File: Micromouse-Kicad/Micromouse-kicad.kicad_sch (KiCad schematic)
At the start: 73 parts, among them J1 SWD, J2 USB_B_Micro, J3 UARTBTH, J4 Batería, SW1 RST, SW2 BootSwitch, SW3 PowerSwitch, SW4 BTN, U1 STM32F405RGT6, U2 LM7805_TO220, U3 AMS1117-3.3, U4 SRV05-4, U5 MPU-6500, U6 DRV8833PWPR, Y1 8MHz

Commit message: Esquemático con componentes básicos
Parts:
- removed H1: M1+, symbol Mechanical:MountingHole_Pad
- removed H2: M1-, symbol Mechanical:MountingHole_Pad
- removed H3: M2+, symbol Mechanical:MountingHole_Pad
- removed H4: M2-, symbol Mechanical:MountingHole_Pad
- added C1, C2, C5, C6: 4.7uF, symbol Device:C_Small
- added C3, C4, C7, C8: 0.1uF, symbol Device:C_Small
- added J5: VL6180x, symbol Connector_Generic:Conn_01x07
- added J6: MotorEncodL, symbol Connector_Generic:Conn_01x06
- added J7: MotorEncodR, symbol Connector_Generic:Conn_01x06
- added Q1, Q2, Q3, Q4: BS170, digikey-footprints:TO-92-3, symbol dk_Transistors-FETs-MOSFETs-Single:BS170
- added R10, R17, R18, R9: 51, symbol Device:R_Small
- added R11, R12, R19, R20: 1.8K, symbol Device:R_Small
- added R13, R14, R5, R6: 100, symbol Device:R_Small
- added R15, R16, R7, R8: 47K, symbol Device:R_Small
- added U10, U7, U8, U9: TCRT5000, TCRT5000-Footprint:OPTO_TCRT5000, symbol TCRT5000:TCRT5000
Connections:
- net +3.3V: now also C1.1, C2.1, C3.1, C4.1, C5.1, C6.1, C7.1, C8.1, J5.1 (Pin_1), J6.4 (Pin_4), J7.4 (Pin_4), R10.2, R17.2, R18.2, R9.2, U10.COLL, U7.COLL, U8.COLL, U9.COLL
- net GND: now also C1.2, C2.2, C3.2, C4.2, C5.2, C6.2, C7.2, C8.2, J5.3 (Pin_3), J6.1 (Pin_1), J7.1 (Pin_1), Q1.3 (S), Q2.3 (S), Q3.3 (S), Q4.3 (S), R11.1, R12.1, R15.1, R16.1, R19.1, R20.1, R7.1, R8.1
- net I2C2_SCL: now also J5.6 (Pin_6)
- net I2C2_SDA: now also J5.7 (Pin_7)
- net LED1: no longer U1.8 (PC0)
- net LED2: no longer U1.9 (PC1)
- net LED3: no longer U1.10 (PC2)
- net LED4: no longer U1.11 (PC3)
- net LED5: no longer U1.24 (PC4)
- net LED6: no longer U1.25 (PC5)
- net FR_Emitter: now reaches U1.16 (PA2)
- net FR_Emitter: now also R5.1
- net FL_Emitter: now reaches U1.17 (PA3)
- net FL_Emitter: now also R13.1
- net R_Emitter: now reaches U1.20 (PA4)
- net R_Emitter: now also R6.1
- net L_Emitter: now reaches U1.21 (PA5)
- net L_Emitter: now also R14.1
- net TIM1_CH1: now reaches U1.41 (PA8)
- net TIM1_CH1: now also J7.3 (Pin_3)
- net TIM1_CH2: now reaches U1.42 (PA9)
- net TIM1_CH2: now also J7.2 (Pin_2)
- net ML1: now reaches U1.58 (PB6)
- net ML1: now also U6.16 (AIN1)
- net ML2: now reaches U1.59 (PB7)
- net ML2: now also U6.15 (AIN2)
- net MR1: now reaches U1.61 (PB8)
- net MR1: now also U6.9 (BIN1)
- net MR2: now reaches U1.62 (PB9)
- net MR2: now also U6.10 (BIN2)
- net OutMR2: now reaches U6.5 (BOUT2)
- net OutMR2: now also J7.5 (Pin_5)
- net OutML1: now reaches U6.2 (AOUT1)
- net OutML1: now also J6.6 (Pin_6)
- net OutML2: now reaches U6.4 (AOUT2)
- net OutML2: now also J6.5 (Pin_5)
- net OutMR1: now reaches U6.7 (BOUT1)
- net OutMR1: now also J7.6 (Pin_6)
- net M1+ renamed TIM8_CH1
- net TIM8_CH1: now also J6.3 (Pin_3); no longer U6.16 (AIN1)
- net M1- renamed TIM8_CH2
- net TIM8_CH2: now also J6.2 (Pin_2); no longer U6.15 (AIN2)
- net M2+: no longer names the net of U1.39 (PC8)
- net M2+: no longer U6.9 (BIN1)
- net M2-: no longer names the net of U1.40 (PC9)
- net M2-: no longer U6.10 (BIN2)
- new net: Q2.2 (G), R6.2, R8.2
- new net: R18.1, U10.A
- new net: Q3.1 (D), U9.CATH
- new net: Q3.2 (G), R13.2, R15.2
- new net: Q4.2 (G), R14.2, R16.2
- new net: Q1.2 (G), R5.2, R7.2
- new net: R9.1, U7.A
- new net: Q1.1 (D), U7.CATH
- new net: Q4.1 (D), U10.CATH
- new net: R17.1, U9.A
- new net: R10.1, U8.A
- new net: Q2.1 (D), U8.CATH
- new net FL_Reciever: R19.2, U1.9 (PC1), U9.E
- new net FR_Reciever: R11.2, U1.8 (PC0), U7.E
- new net L_Reciever: R20.2, U1.11 (PC3), U10.E
- new net R_Reciever: R12.2, U1.10 (PC2), U8.E
- no-connect marks 14 -> 17
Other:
- note added: "IR Sensors"
- note added: "STM32"
- note added: "Sensor distancia - Frontal"
- moved on the sheet: CH1, CH2, D2, J2, J4, RB2, RU1, RU2, RU3, U1, Y1

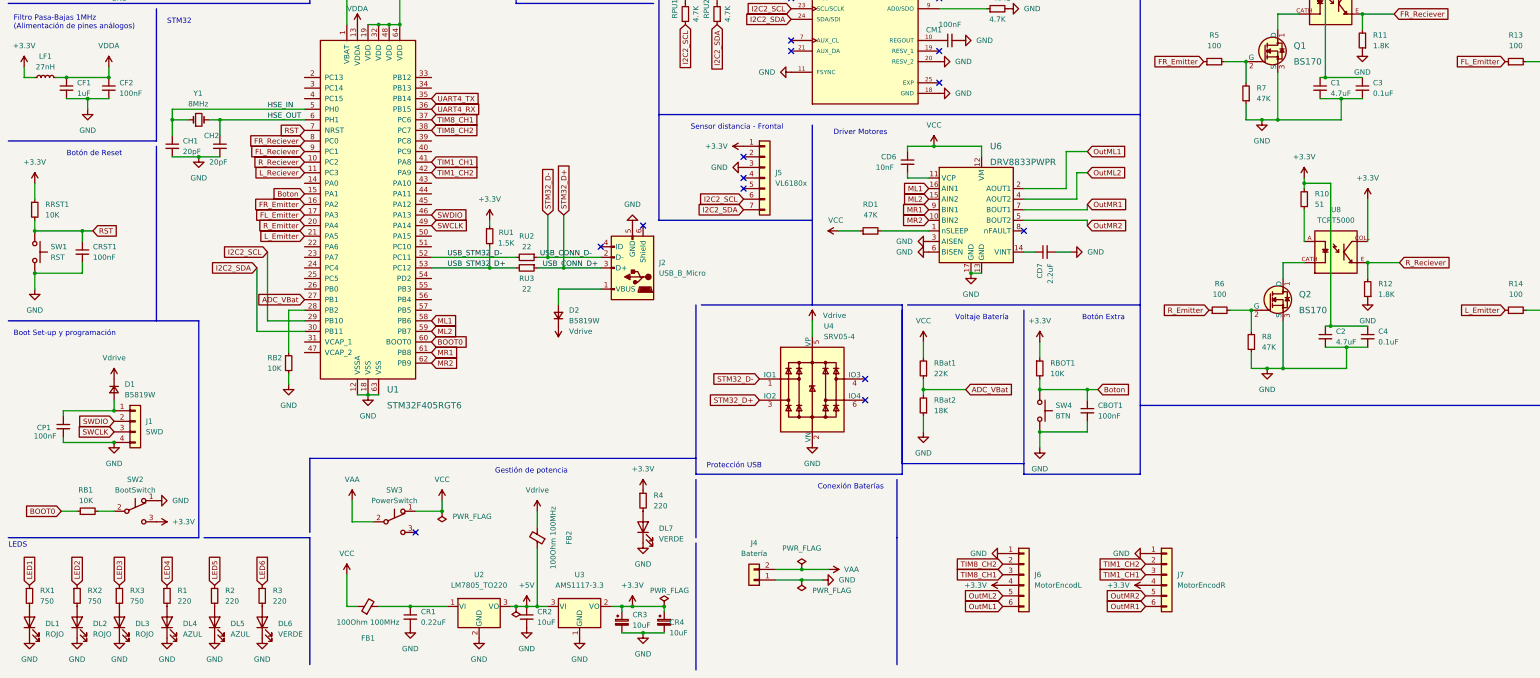
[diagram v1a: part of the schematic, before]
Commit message: Huellas agregadas
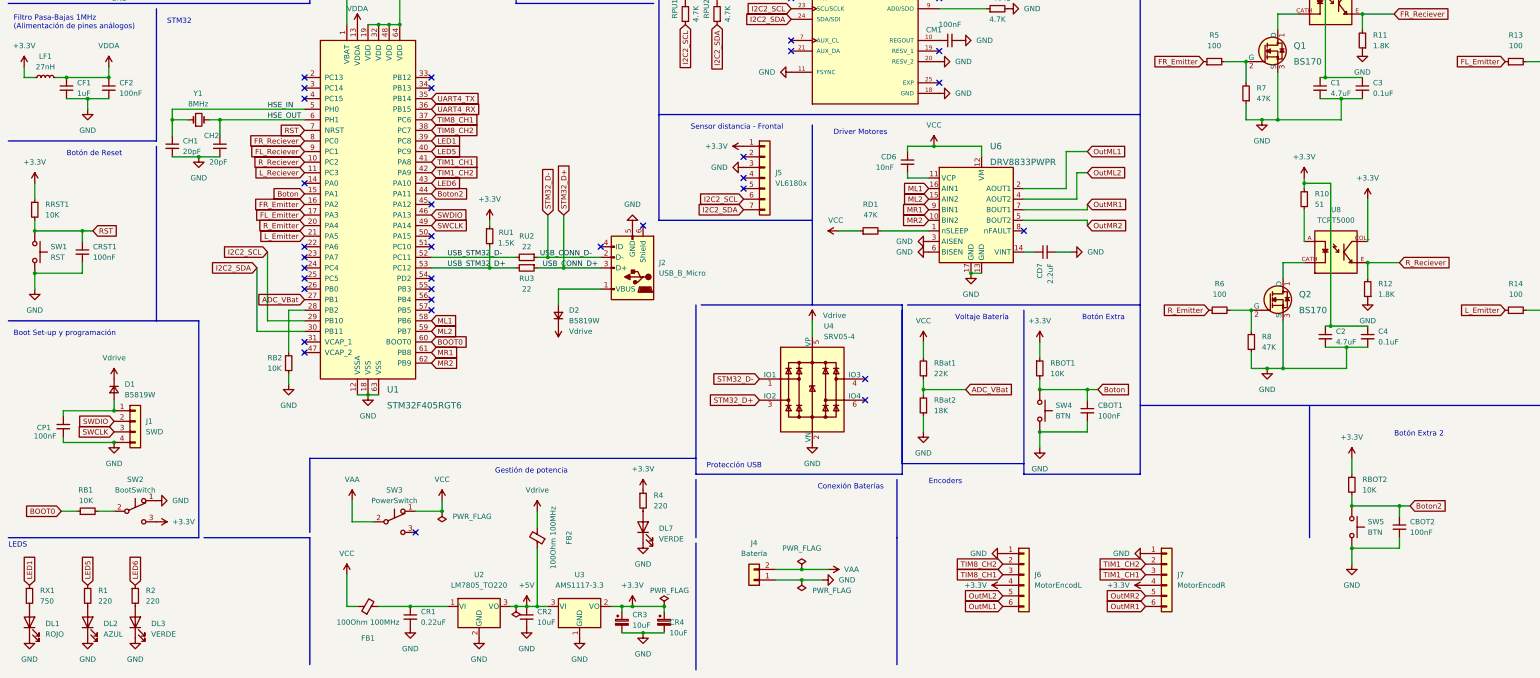
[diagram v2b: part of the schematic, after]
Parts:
- removed DL4, DL5: AZUL, symbol Device:LED
- removed DL6: VERDE, symbol Device:LED
- removed R3: 220, symbol Device:R_Small
- removed RX2, RX3: 750, symbol Device:R_Small
- added CBOT2: 100nF, Capacitor_SMD:C_0402_1005Metric, symbol Device:C_Small
- added RBOT2: 10K, Resistor_SMD:R_0402_1005Metric, symbol Device:R_Small
- added SW5: BTN, Button_Switch_THT:SW_PUSH_6mm_H5mm, symbol Switch:SW_Push
- C1, C2, C3, C4, C5, C6, C7, C8, CBOT1, CD1, CD2, CD3, CD4, CD5, CD6, CD7, CDR1, CF1, CF2, CH1, CH2, CM1, CM2, CM3, CP1, CRST1: footprint (none) -> Capacitor_SMD:C_0402_1005Metric
- CR1, CR2, CR3, CR4: footprint (none) -> Capacitor_SMD:C_1206_3216Metric
- D1, D2: footprint (none) -> Diode_SMD:D_SOD-123
- DL1, DL7: footprint (none) -> LED_SMD:LED_0603_1608Metric
- DL2: value ROJO -> AZUL; footprint (none) -> LED_SMD:LED_0603_1608Metric
- DL3: value ROJO -> VERDE; footprint (none) -> LED_SMD:LED_0603_1608Metric
- FB1, FB2: footprint (none) -> Inductor_SMD:L_0805_2012Metric
- J1: footprint (none) -> Connector_PinHeader_2.54mm:PinHeader_1x04_P2.54mm_Vertical
- J2: footprint (none) -> HUELLAS:MICRO-USB-SMD_5P-P0.65-H-F_MICRO5.9MMUSB
- J3: footprint (none) -> Connector_PinSocket_2.54mm:PinSocket_1x06_P2.54mm_Vertical
- J4: footprint (none) -> HUELLAS:AMASS_XT60-M
- J5: footprint (none) -> Connector_PinSocket_2.54mm:PinSocket_1x07_P2.54mm_Vertical
- J6, J7: footprint (none) -> Connector_JST:JST_XH_B6B-XH-A_1x06_P2.50mm_Vertical
- LF1: footprint (none) -> Inductor_SMD:L_0402_1005Metric
- R1, R2, RX1: footprint (none) -> Resistor_SMD:R_0603_1608Metric
- R10, R11, R12, R13, R14, R15, R16, R17, R18, R19, R20, R4, R5, R6, R7, R8, R9, RB1, RB2, RBOT1, RBat1, RBat2, RD1, RM1, RPU1, RPU2, RRST1, RU1, RU2, RU3: footprint (none) -> Resistor_SMD:R_0402_1005Metric
- SW1, SW4: footprint (none) -> Button_Switch_THT:SW_PUSH_6mm_H5mm
- SW2, SW3: footprint (none) -> HUELLAS:Switch_Slide
- U2: footprint Package_TO_SOT_THT:TO-220-3_Vertical -> Package_TO_SOT_THT:TO-220-3_Horizontal_TabDown
- Y1: footprint (none) -> Crystal:Crystal_SMD_5032-2Pin_5.0x3.2mm
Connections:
- net LED4 is gone; now on net LED5: R1.1
- net +3.3V: now also RBOT2.1
- net GND: now also CBOT2.2, SW5.2
- net LED1: now also U1.39 (PC8)
- net LED5: now also U1.40 (PC9); no longer R2.1
- net LED6: now also R2.1, U1.43 (PA10)
- net Boton2: now reaches U1.44 (PA11)
- net Boton2: now also CBOT2.1, RBOT2.2, SW5.1
- net at DL3.2 (A): now also R2.2
- net at R1.2: now also DL2.2 (A)
- no-connect marks 17 -> 37
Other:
- note added: "Botón Extra 2"
- note added: "Encoders"

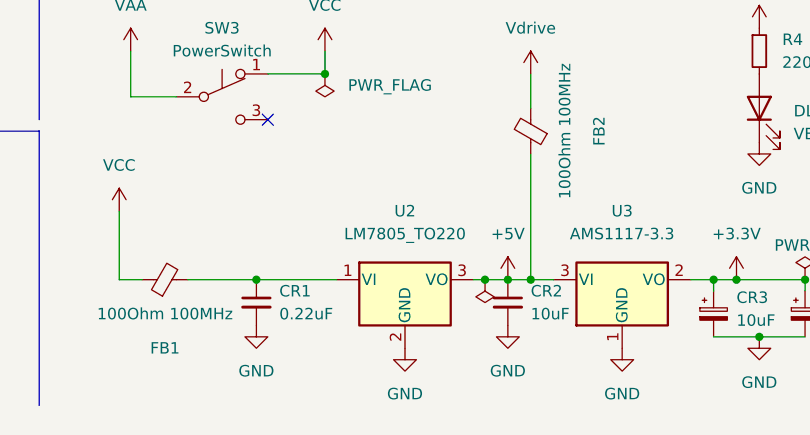
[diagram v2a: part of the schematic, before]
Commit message: Motores routeados
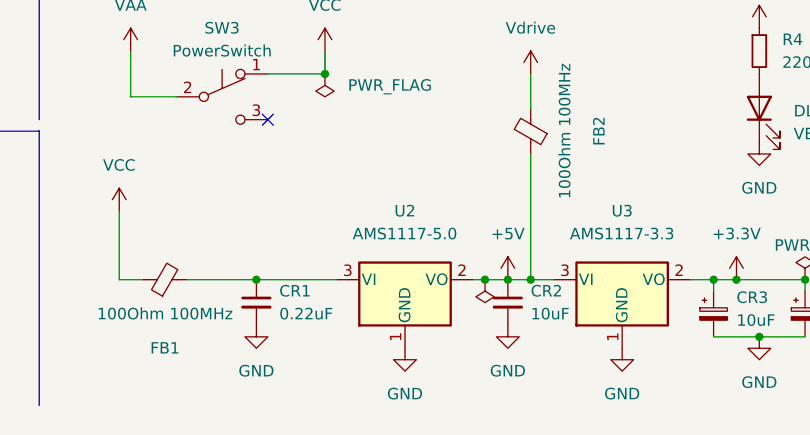
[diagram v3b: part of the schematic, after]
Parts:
- removed U2: LM7805_TO220, Package_TO_SOT_THT:TO-220-3_Horizontal_TabDown, symbol Regulator_Linear:LM7805_TO220
- added U2: AMS1117-5.0, Package_TO_SOT_SMD:SOT-223-3_TabPin2, symbol Regulator_Linear:AMS1117-5.0
- RU2, RU3: footprint Resistor_SMD:R_0402_1005Metric -> Resistor_SMD:R_0603_1608Metric
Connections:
- net +5V: now also U2.2 (VO)
- net GND: now also U2.1 (GND)
- net at CR1.1, FB1.2: now also U2.3 (VI)
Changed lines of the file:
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@@
     (property "Reference" "RU2" (id 0) (at 137.16 93.98 90))
     (property "Value" "22" (id 1) (at 137.16 96.52 90))
-    (property "Footprint" "Resistor_SMD:R_0402_1005Metric" (id 2) (at 137.16 99.06 0)
+    (property "Footprint" "Resistor_SMD:R_0603_1608Metric" (id 2) (at 137.16 99.06 0)
       (effects (font (size 1.27 1.27)) hide)
     )
@@
     (pin "2")
   )
+  (symbol (lib_id "Regulator_Linear:AMS1117-5.0") (at 125.73 182.88 0) (unit 1)
+    (in_bom yes) (on_board yes) (fields_autoplaced)
+    (property "Reference" "U2" (id 0) (at 125.73 175.26 0))
+    (property "Value" "AMS1117-5.0" (id 1) (at 125.73 177.8 0))
+    (property "Footprint" "Package_TO_SOT_SMD:SOT-223-3_TabPin2" (id 2) (at 125.73 177.8 0)
+      (effects (font (size 1.27 1.27)) hide)
+    )
+    (property "Datasheet" "http://www.advanced-monolithic.com/pdf/ds1117.pdf" (id 3) (at 128.27 189.23 0)
+      (effects (font (size 1.27 1.27)) hide)
+    )
+    (pin "1")
+    (pin "2")
+    (pin "3")
+  )
   (symbol (lib_id "Device:R_Small") (at 31.75 180.34 0) (unit 1)
     (in_bom yes) (on_board yes) (fields_autoplaced)
@@
     (pin "1")
   )
-  (symbol (lib_id "Regulator_Linear:LM7805_TO220") (at 125.73 182.88 0) (unit 1)
-    (in_bom yes) (on_board yes) (fields_autoplaced)
-    (property "Reference" "U2" (id 0) (at 125.73 175.26 0))
-    (property "Value" "LM7805_TO220" (id 1) (at 125.73 177.8 0))
-    (property "Footprint" "Package_TO_SOT_THT:TO-220-3_Horizontal_TabDown" (id 2) (at 125.73 177.165 0)
-      (effects (font (size 1.27 1.27) italic) hide)
-    )
-    (property "Datasheet" "https://www.onsemi.cn/PowerSolutions/document/MC7800-D.PDF" (id 3) (at 125.73 184.15 0)
-      (effects (font (size 1.27 1.27)) hide)
-    )
-    (pin "1")
-    (pin "2")
-    (pin "3")
-  )
   (symbol (lib_id "Device:R_Small") (at 260.35 125.73 0) (unit 1)
     (in_bom yes) (on_board yes) (fields_autoplaced)
@@
     (property "Reference" "RU3" (id 0) (at 137.16 104.14 90))
     (property "Value" "22" (id 1) (at 137.16 106.68 90))
-    (property "Footprint" "Resistor_SMD:R_0402_1005Metric" (id 2) (at 137.16 101.6 0)
+    (property "Footprint" "Resistor_SMD:R_0603_1608Metric" (id 2) (at 137.16 101.6 0)
       (effects (font (size 1.27 1.27)) hide)
     )
@@
     )
     (path "/0195a2d3-1de4-42de-a340-422e6c480b4d"
-      (reference "RU2") (unit 1) (value "22") (footprint "Resistor_SMD:R_0402_1005Metric")
+      (reference "RU2") (unit 1) (value "22") (footprint "Resistor_SMD:R_0603_1608Metric")
     )
     (path "/ba43c075-ab2d-4100-bfe1-250946ffa469"
-      (reference "RU3") (unit 1) (value "22") (footprint "Resistor_SMD:R_0402_1005Metric")
+      (reference "RU3") (unit 1) (value "22") (footprint "Resistor_SMD:R_0603_1608Metric")
     )
     (path "/a5ccd16c-0207-46ed-a536-7bf8b96e3f2b"
@@
       (reference "U1") (unit 1) (value "STM32F405RGT6") (footprint "digikey-footprints:LQFP-64_10x10mm")
     )
-    (path "/aa97be75-a68c-43c0-9616-011c0f01b323"
-      (reference "U2") (unit 1) (value "LM7805_TO220") (footprint "Package_TO_SOT_THT:TO-220-3_Horizontal_TabDown")
+    (path "/4ed330c9-c06d-4fe6-b2f1-bba8aa41c34a"
+      (reference "U2") (unit 1) (value "AMS1117-5.0") (footprint "Package_TO_SOT_SMD:SOT-223-3_TabPin2")
     )
     (path "/d75d7916-de59-44ed-96c4-f44890bac7bd"

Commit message: Casi todo routeado
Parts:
- R4: footprint Resistor_SMD:R_0402_1005Metric -> Resistor_SMD:R_0603_1608Metric
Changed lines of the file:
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@@
       (effects (font (size 1.27 1.27)) (justify left))
     )
-    (property "Footprint" "Resistor_SMD:R_0402_1005Metric" (id 2) (at 165.1 157.48 0)
+    (property "Footprint" "Resistor_SMD:R_0603_1608Metric" (id 2) (at 165.1 157.48 0)
       (effects (font (size 1.27 1.27)) hide)
     )
@@
     )
     (path "/45c613f9-aec8-424a-b480-e2cd3c7f1c41"
-      (reference "R4") (unit 1) (value "220") (footprint "Resistor_SMD:R_0402_1005Metric")
+      (reference "R4") (unit 1) (value "220") (footprint "Resistor_SMD:R_0603_1608Metric")
     )
     (path "/3e5cccc0-5e8e-4d7a-84ba-3564961b6bdd"
